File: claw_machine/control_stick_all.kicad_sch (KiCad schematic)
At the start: 0 parts

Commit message: Rework schematic
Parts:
- added J201: Conn_01x05, symbol Connector_Generic:Conn_01x05
- added R201, R202, R203, R204: 10k, Resistor_SMD:R_0805_2012Metric_Pad1.20x1.40mm_HandSolder, symbol Device:R_US
- added SW201, SW202, SW203, SW204: SW_Push, Button_Switch_THT:SW_PUSH_6mm, symbol Switch:SW_Push
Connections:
- new net +5V: J201.5 (Pin_5), SW201.1, SW202.1, SW203.1, SW204.1
- new net EAST_BTN: J201.2 (Pin_2), R204.2, SW204.2
- new net GND: R201.1, R202.1, R203.1, R204.1
- new net NORTH_BTN: J201.1 (Pin_1), R202.2, SW202.2
- new net SOUTH_BTN: J201.3 (Pin_3), R203.2, SW203.2
- new net WEST_BTN: J201.4 (Pin_4), R201.2, SW201.2
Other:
- removed sheet control_stick_single
- removed sheet control_stick_single1
- removed sheet control_stick_single2
- removed sheet control_stick_single3
- removed sheet control_stick_single4
- note added: "Active High Switches"
- note added: "Order: Never East Soggy Wheat 5V"

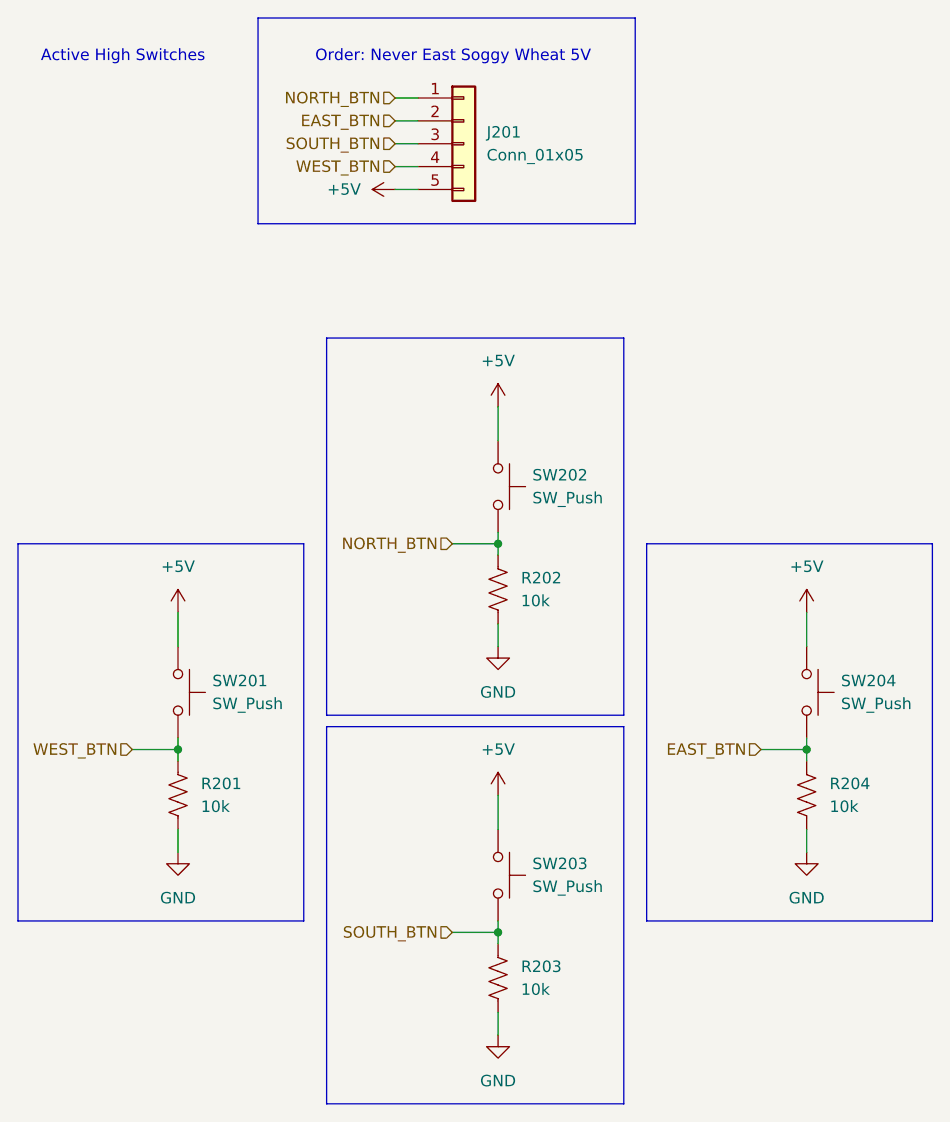
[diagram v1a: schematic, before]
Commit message: Assign footprints
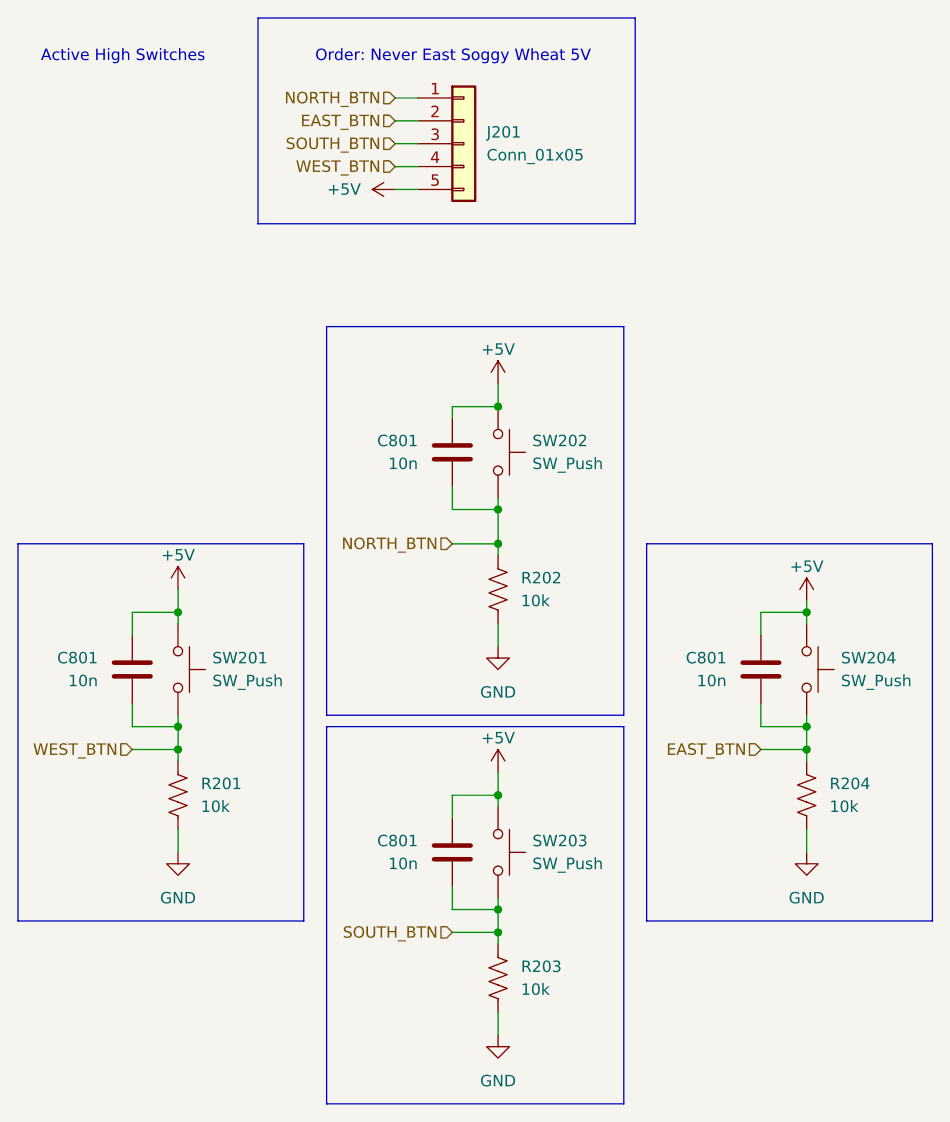
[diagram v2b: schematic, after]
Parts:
- added C801 (x4): 10n, Capacitor_SMD:C_1206_3216Metric_Pad1.33x1.80mm_HandSolder, symbol Device:C
- J201: footprint (none) -> Connector_PinHeader_2.54mm:PinHeader_1x05_P2.54mm_Vertical
- R201, R202, R203, R204: footprint Resistor_SMD:R_0805_2012Metric_Pad1.20x1.40mm_HandSolder -> Resistor_SMD:R_1206_3216Metric_Pad1.30x1.75mm_HandSolder
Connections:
- net +5V: now also C801.1, C801.1, C801.1, C801.1
- net EAST_BTN: now also C801.2
- net NORTH_BTN: now also C801.2
- net SOUTH_BTN: now also C801.2
- net WEST_BTN: now also C801.2
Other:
- moved on the sheet: SW201, SW202, SW203, SW204

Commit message: Tiny bit of PCB work
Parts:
- removed R201, R202, R203, R204: 10k, Resistor_SMD:R_1206_3216Metric_Pad1.30x1.75mm_HandSolder, symbol Device:R_US
- added R105 (x4): 10k, Resistor_SMD:R_1206_3216Metric_Pad1.30x1.75mm_HandSolder, symbol Device:R
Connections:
- net EAST_BTN: now also R105.1
- net GND: now also R105.2, R105.2, R105.2, R105.2
- net NORTH_BTN: now also R105.1
- net SOUTH_BTN: now also R105.1
- net WEST_BTN: now also R105.1

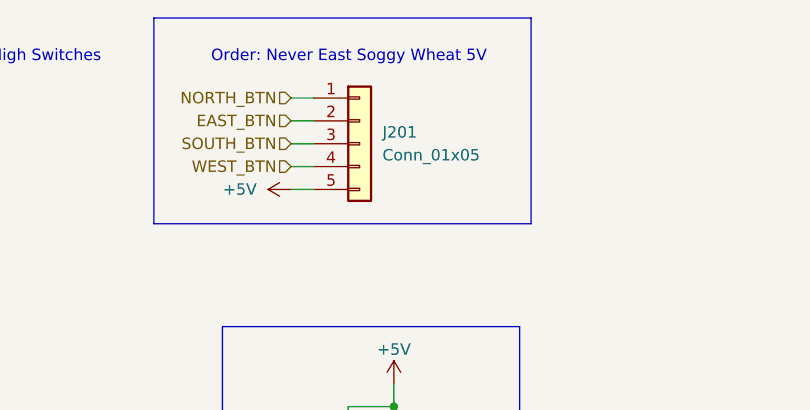
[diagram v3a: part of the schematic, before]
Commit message: Do most of the PCB layout
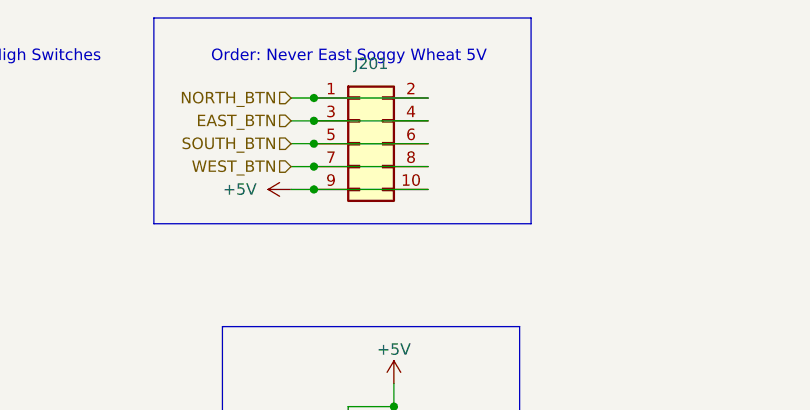
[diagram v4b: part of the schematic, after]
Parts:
- removed J201: Conn_01x05, Connector_PinHeader_2.54mm:PinHeader_1x05_P2.54mm_Vertical, symbol Connector_Generic:Conn_01x05
- added J201: Conn_02x05_Odd_Even, Connector_PinHeader_2.54mm:PinHeader_2x05_P2.54mm_Vertical, symbol Connector_Generic:Conn_02x05_Odd_Even
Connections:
- net +5V: now also J201.10 (Pin_10), J201.9 (Pin_9)
- net EAST_BTN: now also J201.3 (Pin_3), J201.4 (Pin_4)
- net NORTH_BTN: now also J201.1 (Pin_1), J201.2 (Pin_2)
- net SOUTH_BTN: now also J201.5 (Pin_5), J201.6 (Pin_6)
- net WEST_BTN: now also J201.7 (Pin_7), J201.8 (Pin_8)
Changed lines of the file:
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@@
   (junction (at 116.84 58.42) (diameter 0) (color 0 0 0 0)
   )
+  (junction (at 107.95 24.13) (diameter 0) (color 0 0 0 0)
+  )
+  (junction (at 107.95 26.67) (diameter 0) (color 0 0 0 0)
+  )
   (junction (at 116.84 73.66) (diameter 0) (color 0 0 0 0)
   )
+  (junction (at 107.95 34.29) (diameter 0) (color 0 0 0 0)
+  )
   (junction (at 116.84 101.6) (diameter 0) (color 0 0 0 0)
   )
   (junction (at 81.28 81.28) (diameter 0) (color 0 0 0 0)
   )
+  (junction (at 107.95 31.75) (diameter 0) (color 0 0 0 0)
+  )
   (junction (at 151.13 81.28) (diameter 0) (color 0 0 0 0)
   )
+  (junction (at 107.95 29.21) (diameter 0) (color 0 0 0 0)
+  )
   (junction (at 116.84 69.85) (diameter 0) (color 0 0 0 0)
   )
@@
     (stroke (width 0) (type default))
   )
+  (wire (pts (xy 107.95 34.29) (xy 120.65 34.29))
+    (stroke (width 0) (type default))
+  )
   (wire (pts (xy 81.28 81.28) (xy 81.28 82.55))
     (stroke (width 0) (type default))
@@
     (stroke (width 0) (type default))
   )
+  (wire (pts (xy 107.95 29.21) (xy 120.65 29.21))
+    (stroke (width 0) (type default))
+  )
   (wire (pts (xy 116.84 101.6) (xy 116.84 102.87))
     (stroke (width 0) (type default))
@@
     (stroke (width 0) (type default))
   )
+  (wire (pts (xy 107.95 24.13) (xy 120.65 24.13))
+    (stroke (width 0) (type default))
+  )
   (wire (pts (xy 76.2 93.98) (xy 81.28 93.98))
     (stroke (width 0) (type default))
@@
     (stroke (width 0) (type default))
   )
+  (wire (pts (xy 107.95 31.75) (xy 120.65 31.75))
+    (stroke (width 0) (type default))
+  )
   (wire (pts (xy 105.41 24.13) (xy 107.95 24.13))
     (stroke (width 0) (type default))
@@
   )
   (wire (pts (xy 111.76 116.84) (xy 116.84 116.84))
+    (stroke (width 0) (type default))
+  )
+  (wire (pts (xy 107.95 26.67) (xy 120.65 26.67))
     (stroke (width 0) (type default))
   )
@@
         (path "/2e48e9a4-e55f-4bd7-8086-6a8b9c5eabc1/6818ac2a-ce5d-423a-9389-7753b58c3ff7"
           (reference "R204") (unit 1)
+        )
+      )
+    )
+  )
+  (symbol (lib_id "Connector_Generic:Conn_02x05_Odd_Even") (at 113.03 29.21 0) (unit 1)
+    (in_bom yes) (on_board yes) (dnp no)
+    (property "Reference" "J201" (at 114.3 20.32 0)
+      (effects (font (size 1.27 1.27)))
+    )
+    (property "Value" "Conn_02x05_Odd_Even" (at 114.3 20.32 0)
+      (effects (font (size 1.27 1.27)) hide)
+    )
+    (property "Footprint" "Connector_PinHeader_2.54mm:PinHeader_2x05_P2.54mm_Vertical" (at 113.03 29.21 0)
+      (effects (font (size 1.27 1.27)) hide)
+    )
+    (property "Datasheet" "~" (at 113.03 29.21 0)
+      (effects (font (size 1.27 1.27)) hide)
+    )
+    (pin "1")
+    (pin "10")
+    (pin "2")
+    (pin "3")
+    (pin "4")
+    (pin "5")
+    (pin "6")
+    (pin "7")
+    (pin "8")
+    (pin "9")
+    (instances
+      (project "claw_machine"
+        (path "/2e48e9a4-e55f-4bd7-8086-6a8b9c5eabc1/6818ac2a-ce5d-423a-9389-7753b58c3ff7"
+          (reference "J201") (unit 1)
         )
       )
@@
         )
       )
-    )
-  )
-  (symbol (lib_id "Connector_Generic:Conn_01x05") (at 113.03 29.21 0) (unit 1)
-    (in_bom yes) (on_board yes) (dnp no) (fields_autoplaced)
-    (property "Reference" "J201" (at 115.57 27.94 0)
-      (effects (font (size 1.27 1.27)) (justify left))
-    )
-    (property "Value" "Conn_01x05" (at 115.57 30.48 0)
-      (effects (font (size 1.27 1.27)) (justify left))
-    )
-    (property "Footprint" "Connector_PinHeader_2.54mm:PinHeader_1x05_P2.54mm_Vertical" (at 113.03 29.21 0)
-      (effects (font (size 1.27 1.27)) hide)
-    )
-    (property "Datasheet" "~" (at 113.03 29.21 0)
-      (effects (font (size 1.27 1.27)) hide)
-    )
-    (pin "1")
-    (pin "2")
-    (pin "3")
-    (pin "4")
-    (pin "5")
-    (instances
-      (project "claw_machine"
-        (path "/2e48e9a4-e55f-4bd7-8086-6a8b9c5eabc1/6818ac2a-ce5d-423a-9389-7753b58c3ff7"
-          (reference "J201") (unit 1)
-        )
-      )
